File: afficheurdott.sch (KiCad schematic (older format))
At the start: 58 parts

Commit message: Refactoring and more stuff
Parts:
- removed 3k9, 3k?: R, symbol Device:R
- removed J? (x2): Conn_01x03_Female, symbol Connector:Conn_01x03_Female
- removed Q?: BC109, Package_TO_SOT_THT:TO-18-3, symbol Transistor_BJT:BC109
- removed R? (x2): 1k, symbol Device:R
- removed R? (x2): 8k2R, symbol Device:R
- added C?: 100n, symbol Device:C_Small
- added D?: D, symbol Device:D
- added J?: Brake 1, symbol Connector:Conn_01x03_Female
- added J?: Brake 2, symbol Connector:Conn_01x03_Female
- added Q? (x2): BC847, Package_TO_SOT_SMD:SOT-23, symbol Transistor_BJT:BC847
- added R? (x2): 1k, symbol Device:R
- added R? (x2): 3k9, symbol Device:R
- added R? (x2): 8k2, symbol Device:R
- added R? (x7): 10k, symbol Device:R
- C? (x2): value C_Small -> 100n
- C?: value C_Small -> 47p
- C?: value C_Small -> 20u
- C?: value C_Small -> 10u
- D?: value D_Schottky -> D
- J?: value Conn_01x04 -> Pogo pins
- J?: value Conn_01x05_Female -> CAN Controller
- J?: value Conn_01x05_Female -> CAN IOT
- J?: value Conn_01x03_Female -> Accelerator
- J?: value Conn_01x02_Female -> Front Light
- J?: value Conn_01x03_Female -> Rear Light
- L?: value 68mH L -> 68mH
- R?: value 3k9R -> 3k9
- R?: value 8k2R -> 8k2
- R?: value 1kR -> 1k
- R?: value 47kR -> 47k
- R?: value 10R -> 100
- R?: value 50mR -> 50m
- R?: value 2k2R -> 2k2
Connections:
- net 3.3Vo is gone; now on net +3V3: J?.1 (Pin_1), U?.1 (VDD), U?.2 (VO), U?.3 (VCC)
- net pin13 is gone; now on net Accelerator: U?.13 (PA7)
- net +BATT: now also J?.1 (Pin_1), J?.1 (Pin_1); no longer J?.3 (Pin_3), J?.3 (Pin_3), R?.2, U?.7 (CANH)
- net GND: now also C?.2, J?.5 (Pin_5), J?.5 (Pin_5), Q?.2 (E), R?.2, U?.32 (VSSA), C?.2, J?.1 (Pin_1), J?.1 (Pin_1), Q?.2 (E), R?.2, R?.2, R?.2; no longer Q?.3 (C)
- net SWIO: now also R?.2
- net slp_cnt: now reaches U?.15 (PB1)
- net slp_cnt: now also R?.2
- net +3V3: now reaches U?.17 (VDDIO2)
- net +3V3: now also U?.5 (VDDA), R?.1, R?.1, R?.1
- net at U?.19 (PA9): now also R?.2; no longer R?.1
- net at U?.20 (PA10): now also R?.2; no longer R?.1
- net at U?.4 (NRST): now also C?.1, R?.2
- net at U?.8 (PA2): now also R?.2
- net Tx: now reaches U?.1 (D)
- net Tx: now also R?.1
- net Rx: now reaches U?.4 (R)
- net Rx: now also R?.1
- net CANL: now reaches J?.4 (Pin_4), U?.6 (CANL)
- net CANL: now also J?.4 (Pin_4), R?.1; no longer J?.2 (Pin_2), R?.2
- net at U?.8 (Rs): now also R?.1
- net Control: now reaches J?.2 (Pin_2)
- net Control: now also J?.2 (Pin_2), D?.2 (A); no longer J?.4 (Pin_4)
- net +VSW: now reaches J?.3 (Pin_3), Q?.3 (C)
- net +VSW: now also J?.3 (Pin_3), J?.3 (Pin_3)
- net at J?.2 (Pin_2), Q?.3 (C): now also Q?.3 (C); no longer Q?.2 (E)
- net at J?.1 (Pin_1): now also Q?.3 (C)
- net at R?.1, R?.2: now also Q?.1 (B)
- net at C?.2, U?.5 (FB): now also R?.1, R?.2; no longer C?.2, R?.2
- net EN: now reaches U?.6 (EN)
- net EN: now also Q?.3 (C), R?.1
- net at Q?.1 (B): now also R?.2; no longer R?.1
- net at D?.1 (K): now also R?.1; no longer R?.2
- removed net -BATT: J?.1 (Pin_1), J?.5 (Pin_5)
- net SWCLOCK renamed SWCLK
- net SWCLK: now also R?.2
- net pin10 renamed Accelerator
- net Accelerator: no longer U?.10 (PA4)
- net pin11 renamed Brake2
- net Brake2: now also R?.1, R?.2
- net pin14 renamed Front_light
- net pin18 renamed pwr_snr
- net pin21: no longer names the net of U?.21 (PA11)
- net pin21: now also R?.2
- net pin22: no longer names the net of U?.22 (PA12)
- net pin22: now also R?.2
- net pin28 renamed DIN
- net pin29 renamed CLK
- net pin30 renamed STB
- new net: J?.2 (Pin_2), R?.1 (x2)
- new net: Q?.1 (B), R?.1, R?.1
- new net: Q?.2 (E), R?.2
- new net: D?.1 (K), R?.2
- new net Brake1: R?.1, R?.2, U?.10 (PA4)
- new net CANH: J?.3 (Pin_3), J?.3 (Pin_3), R?.1, U?.7 (CANH)
- no-connect marks 0 -> 6
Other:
- note added: "red black green"
- note added: "red yellow green"
- note removed: "Accelerator (red yellow green)"
- note removed: "Brake 1 (red black green)"
- note removed: "Brake 2 (red black green)"
- note removed: "Front light"
- note removed: "Julet 3 pins, yellow"
- note removed: "Julet 5 court"
- note removed: "Julet 5 long"
- note removed: "Programming port"
- moved on the sheet: C?, D?, J?, L?, Q?, R?, U?

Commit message: Added connctions, correction small errors
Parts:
- removed Q?: Q_NPN_BEC, symbol Device:Q_NPN_BEC
- removed Q?: BC847, Package_TO_SOT_SMD:SOT-23, symbol Transistor_BJT:BC847
- removed R?: 1kR, symbol Device:R
- removed R?: 10kR, symbol Device:R
- added C?: 100n, symbol Device:C_Small
- added D?: D, symbol Device:D
- added Q?: L8550HQLT1, symbol Device:Q_PNP_BEC
- added R? (x3): 1k, symbol Device:R
- added R?: 100k, symbol Device:R
- J?: value Pogo pins -> Prog
- J?: value Conn_01x04_Female -> ??
- Q?: value Q_PNP_BEC -> L8550HQLT1
- R?: value 200kR -> 200k
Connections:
- net +6V is gone; now on an unnamed net: J?.2 (Pin_2)
- net +BATT: now also J?.1 (Pin_1), R?.1
- net +VSW: now also J?.1 (Pin_1), J?.1 (Pin_1), J?.1 (Pin_1); no longer J?.3 (Pin_3), J?.3 (Pin_3), J?.3 (Pin_3)
- net Control: now also D?.1 (K); no longer D?.2 (A)
- net EN: now also Q?.3 (C), R?.2
- net GND: now also D?.2 (A), J?.3 (Pin_3), J?.3 (Pin_3), J?.3 (Pin_3), R?.2, C?.2; no longer J?.1 (Pin_1), J?.1 (Pin_1), J?.1 (Pin_1)
- net unk_B: now reaches U?.12 (PA6)
- net unk_B: now also R?.2
- net ON: now reaches U?.9 (PA3)
- net ON: now also D?.2 (A)
- net at J?.1 (Pin_1): now also R?.1
- net at J?.4 (Pin_4): now also R?.1
- net at Q?.3 (C): no longer J?.1 (Pin_1)
- net Rear_light: now reaches J?.2 (Pin_2)
- net Rear_light: now also R?.1
- net at D?.1 (K): now also R?.1, C?.1, Q?.2 (E), R?.2
- net at R?.1: now also R?.2, Q?.1 (B); no longer R?.1
- net at R?.2: now also D?.2 (A); no longer D?.1 (K)
- net pin27: no longer names the net of R?.2
- net pin27: no longer U?.27 (PB4)
- net pin31: no longer names the net of R?.1, U?.31 (PB8)
- new net: D?.1 (K), R?.1
- new net unk_A: R?.2, U?.27 (PB4)
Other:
- note added: "Not used"
- note added: "black green red"
- note added: "black yellow red"
- note removed: "CAUTION : Connectors are organized in order seen by user when facing LED screen !"
- note removed: "red black green"
- note removed: "red yellow green"
- moved on the sheet: C?, D?, J?, Q?, R?, U?

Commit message: Done
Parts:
- removed J? (x2): Conn_01x02_Female, symbol Connector:Conn_01x02_Female
- removed Q? (x2): BC109, Package_TO_SOT_THT:TO-18-3, symbol Transistor_BJT:BC109
- removed Q?: Q_NPN_BEC, symbol Device:Q_NPN_BEC
- removed R? (x3): 10kR, symbol Device:R
- removed R? (x2): 1kR, symbol Device:R
- added C?: 47u, symbol Device:CP
- added C?: 220u, symbol Device:CP
- added J?: Out A, symbol Connector:Conn_01x02_Female
- added J?: Out B, symbol Connector:Conn_01x02_Female
- added J?: LED display, symbol Connector_Generic:Conn_01x14
- added L?: E907067, symbol Device:L_Core_Ferrite_Coupled_Small
- added Q? (x2): BC847, Package_TO_SOT_SMD:SOT-23, symbol Transistor_BJT:BC847
- added R? (x2): 1k, symbol Device:R
- added R? (x2): 10k, symbol Device:R
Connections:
- net +5V: now also C?.1, J?.1 (Pin_1), J?.1 (Pin_1)
- net +BATT: now also C?.1
- net CANH: now also L?.1; no longer J?.3 (Pin_3), J?.3 (Pin_3)
- net CANL: now also L?.3; no longer J?.4 (Pin_4), J?.4 (Pin_4)
- net GND: now also C?.2, C?.2, Q?.2 (E), Q?.2 (E), R?.2, R?.2
- net at U?.10 (GRID6): now also J?.14 (Pin_14)
- net at U?.11 (GRID5): now also J?.13 (Pin_13)
- net at U?.13 (GRID4): now also J?.12 (Pin_12)
- net at U?.14 (GRID3): now also J?.11 (Pin_11)
- net at U?.16 (GRID2): now also J?.10 (Pin_10)
- net at U?.17 (GRID1): now also J?.9 (Pin_9)
- net at U?.2 (SEG1): now also J?.1 (Pin_1)
- net at U?.3 (SEG2): now also J?.2 (Pin_2)
- net at U?.4 (SEG3): now also J?.3 (Pin_3)
- net at U?.5 (SEG4): now also J?.4 (Pin_4)
- net at U?.6 (SEG5): now also J?.5 (Pin_5)
- net at U?.7 (SEG6): now also J?.6 (Pin_6)
- net at U?.8 (SEG7): now also J?.7 (Pin_7)
- net at U?.9 (SEG8): now also J?.8 (Pin_8)
- net pin25 renamed out_B
- net out_B: now also R?.1
- net pin26 renamed out_A
- net out_A: now also R?.1
- new net: J?.3 (Pin_3), J?.3 (Pin_3), L?.2
- new net: J?.4 (Pin_4), J?.4 (Pin_4), L?.4
- new net: Q?.1 (B), R?.1, R?.2 (x2)
- new net: J?.2 (Pin_2), Q?.3 (C) (x2)
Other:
- note added: "Connectors"
- note added: "Not sure of that.\nTwo A12 in SOT23\nare tied between\nCANx and GND"
- moved on the sheet: C?, D?, J?, L?, Q?, R?, U?

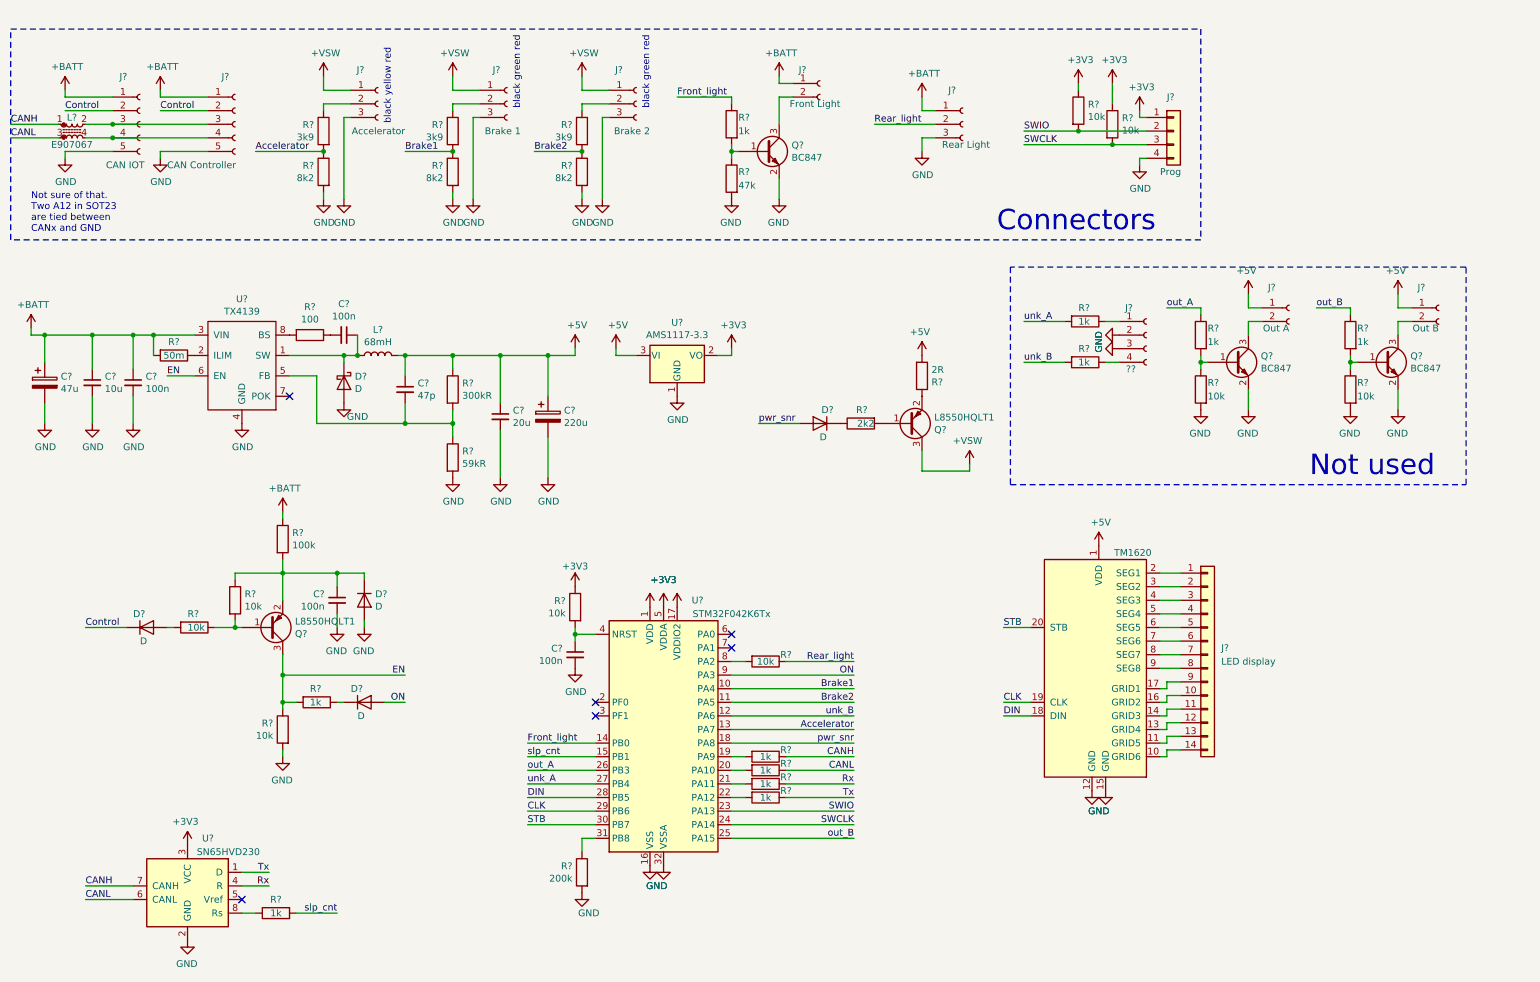
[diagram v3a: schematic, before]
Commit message: More comments
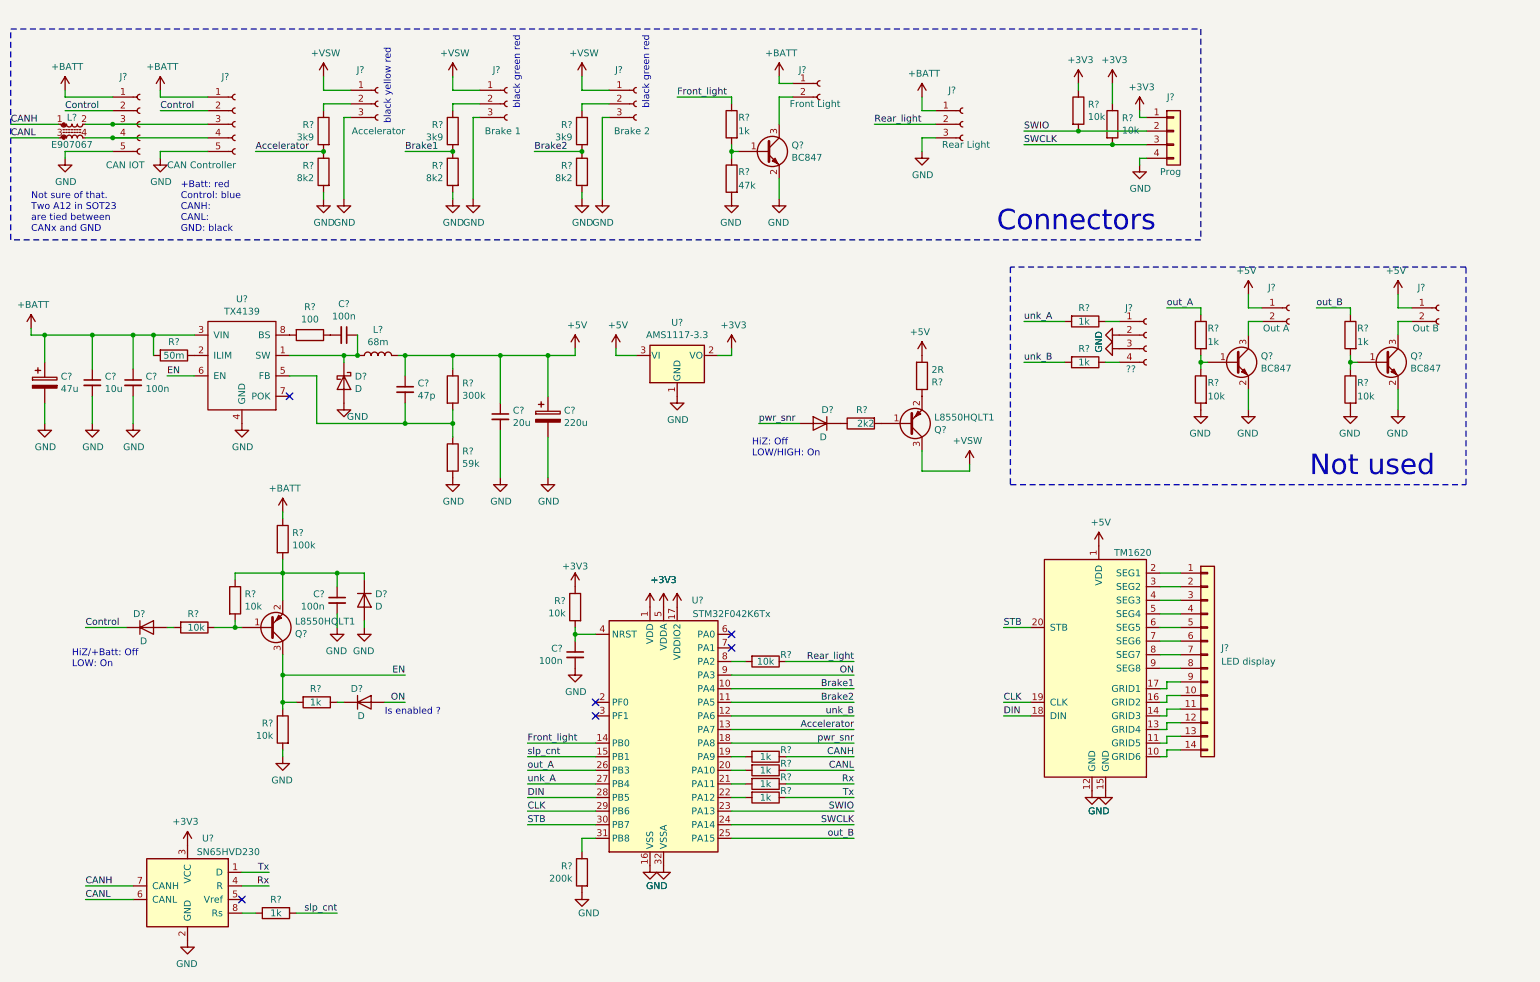
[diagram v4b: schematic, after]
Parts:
- L?: value 68mH -> 68m
- R?: value 300kR -> 300k
- R?: value 59kR -> 59k
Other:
- note added: "+Batt: red\nControl: blue\nCANH:\nCANL:\nGND: black"
- note added: "HiZ/+Batt: Off\nLOW: On"
- note added: "HiZ: Off\nLOW/HIGH: On"
- note added: "Is enabled ?"
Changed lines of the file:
@@
 P 3750 3150
 F 0 "R?" H 3820 3196 50  0000 L CNN
-F 1 "300kR" H 3820 3105 50  0000 L CNN
+F 1 "300k" H 3820 3105 50  0000 L CNN
 F 2 "" V 3680 3150 50  0001 C CNN
 F 3 "~" H 3750 3150 50  0001 C CNN
@@
 P 3750 3650
 F 0 "R?" H 3820 3696 50  0000 L CNN
-F 1 "59kR" H 3820 3605 50  0000 L CNN
+F 1 "59k" H 3820 3605 50  0000 L CNN
 F 2 "" V 3680 3650 50  0001 C CNN
 F 3 "~" H 3750 3650 50  0001 C CNN
@@
 P 3200 2900
 F 0 "L?" V 3390 2900 50  0000 C CNN
-F 1 "68mH" V 3299 2900 50  0000 C CNN
+F 1 "68m" V 3299 2900 50  0000 C CNN
 F 2 "" H 3200 2900 50  0001 C CNN
 F 3 "~" H 3200 2900 50  0001 C CNN
@@
 	1    0    0    -1
 $EndComp
-Wire Wire Line
-	1350 4900 1050 4900
-Text Label 1050 4900 0    50   ~ 0
-Control
 $Comp
 L Device:R R?
@@
 	1    0    0    -1
 $EndComp
+Text Label 1050 4900 0    50   ~ 0
+Control
+Wire Wire Line
+	1350 4900 1050 4900
+Text Notes 1750 2000 0    50   ~ 0
++Batt: red\nControl: blue\nCANH:\nCANL:\nGND: black
+Text Notes 5950 3650 0    50   ~ 0
+HiZ: Off\nLOW/HIGH: On
+Text Notes 950  5200 0    50   ~ 0
+HiZ/+Batt: Off\nLOW: On
+Text Notes 3250 5550 0    50   ~ 0
+Is enabled ?
 $EndSCHEMATC
